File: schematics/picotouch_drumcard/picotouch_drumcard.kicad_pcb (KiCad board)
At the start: 2 copper layers, 88.9 x 63.5 mm, 73 parts, among them J1 AudioJack4, J2 AudioJack4, J3 AudioJack4, SW1 Capacitive Button, SW10 Capacitive Button, SW11 Capacitive Button, SW12 Capacitive Button, SW13 Capacitive Button, SW14 Capacitive Button, SW15 Capacitive Button, SW16 Capacitive Button, SW17 Capacitive Button, SW2 Capacitive Button, SW3 Capacitive Button, SW4 Capacitive Button, SW5 Capacitive Button, SW6 Capacitive Button, SW7 Capacitive Button, SW8 Capacitive Button, SW9 Capacitive Button, U1 Pico, U2 H11L1S(TA), U3 MCP73831-2-OT, U4 TS20, X1 AFC20-S02ACA-00

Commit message: second
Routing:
- net /TOUCH5: track 49.0 -> 49.6 mm
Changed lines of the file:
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@@
 			(layers "B.Cu" "B.Paste" "B.Mask")
 			(net 48 "unconnected-(J3-PadR2)")
-			(pintype "passive")
+			(pintype "passive+no_connect")
 		)
 		(pad "S" smd rect
@@
 			(net 83 "unconnected-(U1-GPIO18-Pad24)")
 			(pinfunction "GPIO18")
-			(pintype "bidirectional")
+			(pintype "bidirectional+no_connect")
 		)
 		(pad "25" smd rect
@@
 			(layers "B.Cu" "B.Paste" "B.Mask")
 			(net 47 "unconnected-(J2-PadR2)")
-			(pintype "passive")
+			(pintype "passive+no_connect")
 		)
 		(pad "S" smd rect
@@
 	)
 	(segment
-		(start 118.11 33.02)
-		(end 156.48125 33.02)
+		(start 118.872 33.782)
+		(end 116.84 31.75)
 		(width 0.2)
 		(layer "B.Cu")
@@
 	)
 	(segment
-		(start 156.48125 33.02)
-		(end 157.319 33.85775)
+		(start 157.319 33.85775)
+		(end 157.319 34.6025)
 		(width 0.2)
 		(layer "B.Cu")
@@
 	)
 	(segment
-		(start 116.84 31.75)
-		(end 118.11 33.02)
+		(start 133.096 33.782)
+		(end 133.858 33.02)
 		(width 0.2)
 		(layer "B.Cu")
@@
 	)
 	(segment
-		(start 157.319 33.85775)
-		(end 157.319 34.6025)
+		(start 133.858 33.02)
+		(end 156.48125 33.02)
+		(width 0.2)
+		(layer "B.Cu")
+		(net 6)
+	)
+	(segment
+		(start 156.48125 33.02)
+		(end 157.319 33.85775)
+		(width 0.2)
+		(layer "B.Cu")
+		(net 6)
+	)
+	(segment
+		(start 133.096 33.782)
+		(end 118.872 33.782)
 		(width 0.2)
 		(layer "B.Cu")
@@
 	)
 	(segment
+		(start 164.592 38.862)
+		(end 161.869 36.139)
+		(width 0.2)
+		(layer "B.Cu")
+		(net 41)
+	)
+	(segment
 		(start 165.1 42.418)
 		(end 165.1 49.022)
@@
 	)
 	(segment
-		(start 164.592 38.862)
-		(end 161.869 36.139)
-		(width 0.2)
-		(layer "B.Cu")
-		(net 41)
-	)
-	(segment
-		(start 165.1 51.562)
-		(end 165.1 44.958)
+		(start 163.576 42.926)
+		(end 163.576 40.894)
 		(width 0.2)
 		(layer "F.Cu")
@@
 	)
 	(segment
-		(start 165.1 44.958)
-		(end 163.83 43.688)
+		(start 163.576 40.894)
+		(end 162.56 39.878)
 		(width 0.2)
 		(layer "F.Cu")
@@
 	)
 	(segment
-		(start 163.83 43.688)
-		(end 163.83 41.148)
+		(start 162.56 39.878)
+		(end 162.56 38.862)
 		(width 0.2)
 		(layer "F.Cu")
@@
 	)
 	(segment
-		(start 163.83 41.148)
-		(end 162.56 39.878)
+		(start 165.1 51.562)
+		(end 165.1 44.45)
 		(width 0.2)
 		(layer "F.Cu")
@@
 	)
 	(segment
-		(start 162.56 39.878)
-		(end 162.56 38.862)
+		(start 119.38 67.31)
+		(end 123.952 71.882)
 		(width 0.2)
 		(layer "F.Cu")
@@
 	)
 	(segment
-		(start 119.38 67.31)
-		(end 123.952 71.882)
+		(start 165.1 44.45)
+		(end 163.576 42.926)
 		(width 0.2)
 		(layer "F.Cu")

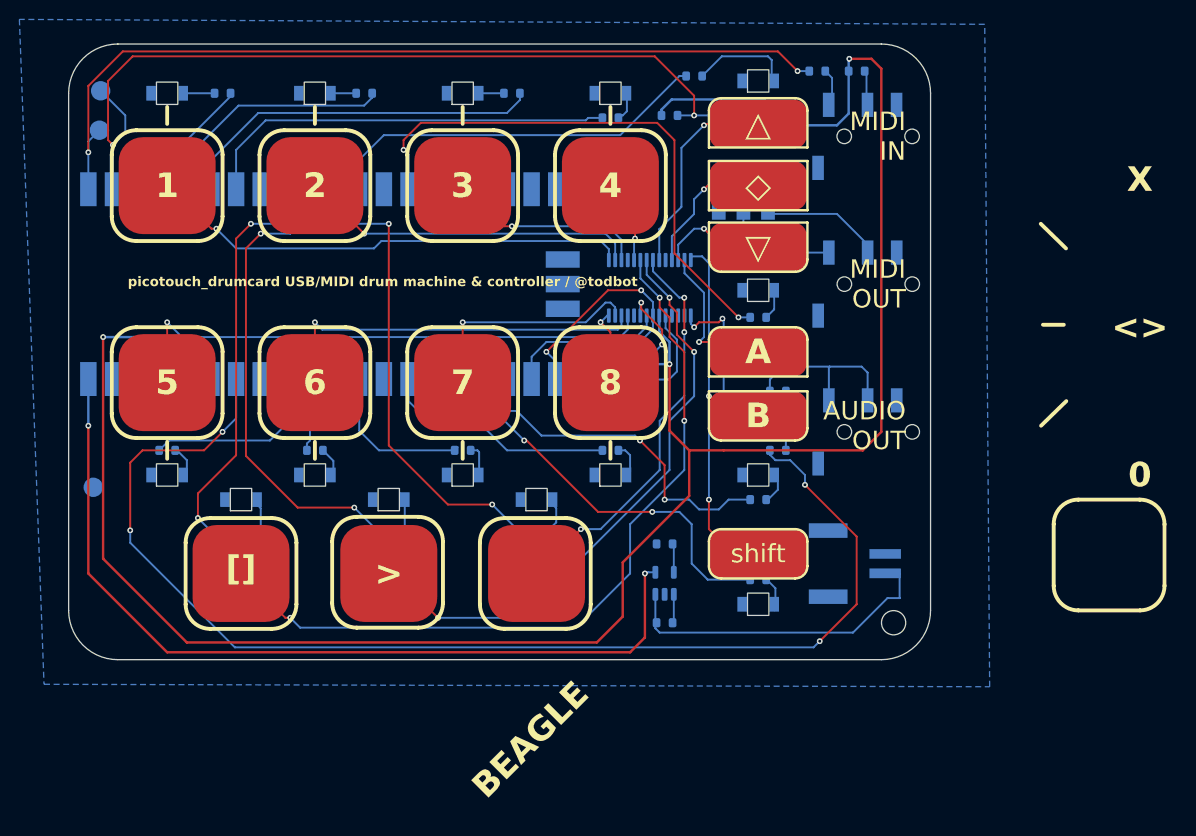
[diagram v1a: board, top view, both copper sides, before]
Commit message: added protection diodes
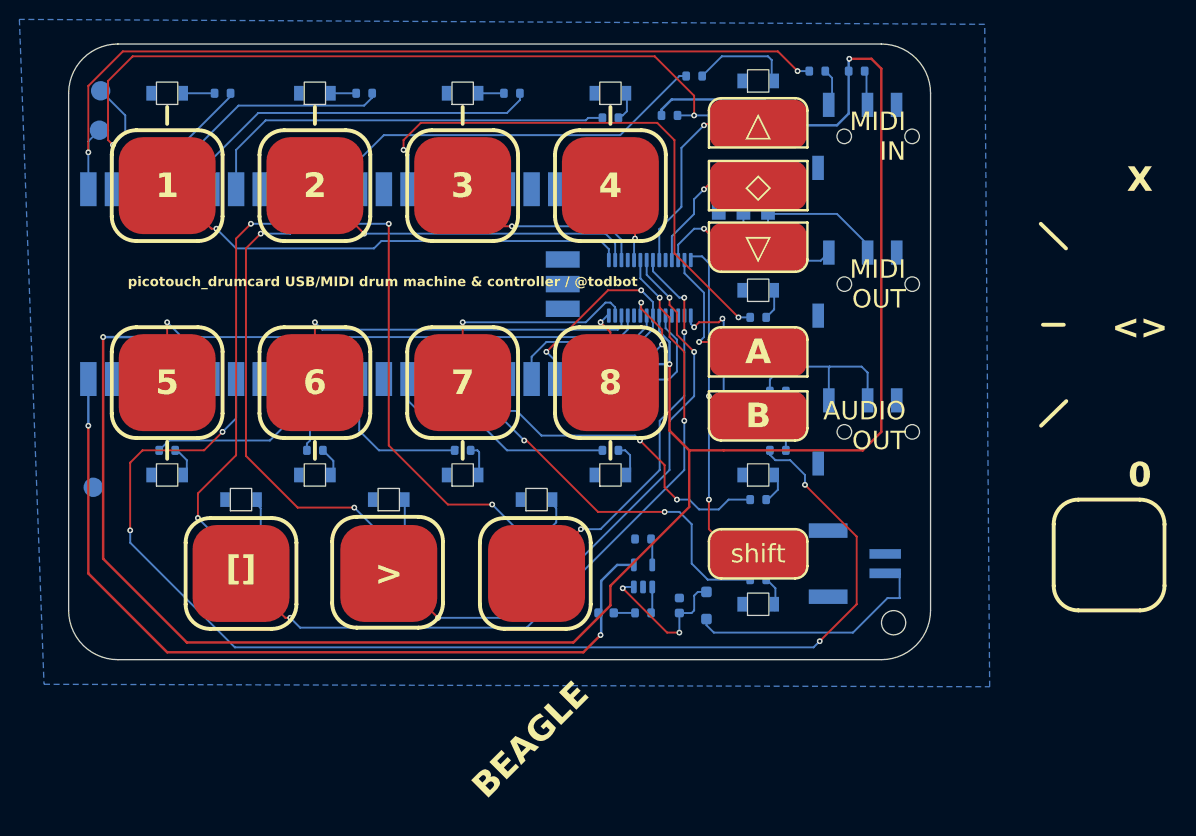
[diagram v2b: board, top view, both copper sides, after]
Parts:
- added C4: 10uF, Capacitor_SMD:C_0603_1608Metric, B.Cu at (164.6, 70.6)
- added D16: 1N4148WT, Diode_SMD:D_SOD-123F, B.Cu at (172.7, 33.7)
- added D17: orange, LED_SMD:LED_0603_1608Metric, B.Cu at (157.0, 71.4)
- added D18: MBR120, Diode_SMD:D_SOD-123F, B.Cu at (167.4, 70.6)
- moved R301 2.44 mm to (160.8, 71.4)
- moved U3 2.35 mm to (160.8, 67.6)
- moved R300 2.28 mm to (160.8, 63.8)
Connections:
- R301 pad 2: +BATT -> Net-(D17-K)
- U3 pad 3: +BATT -> Net-(D18-K)
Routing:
- net Net-(D18-K): track 0.00 -> 15.5 mm, vias 0 -> 2
- net +BATT: track 34.4 -> 26.4 mm
- net Net-(D16-K): track 12.8 -> 16.6 mm
- net /TOUCH9: track 81.7 -> 78.7 mm
- net Net-(D16-A): track 11.8 -> 14.4 mm
- net +5V: track 90.1 -> 87.6 mm
- net Net-(D17-K): track 0.00 -> 2.20 mm
- net +3.3V: track 227.0 -> 225.5 mm
- net /LED14: track 40.5 -> 39.7 mm

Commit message: fix button labels
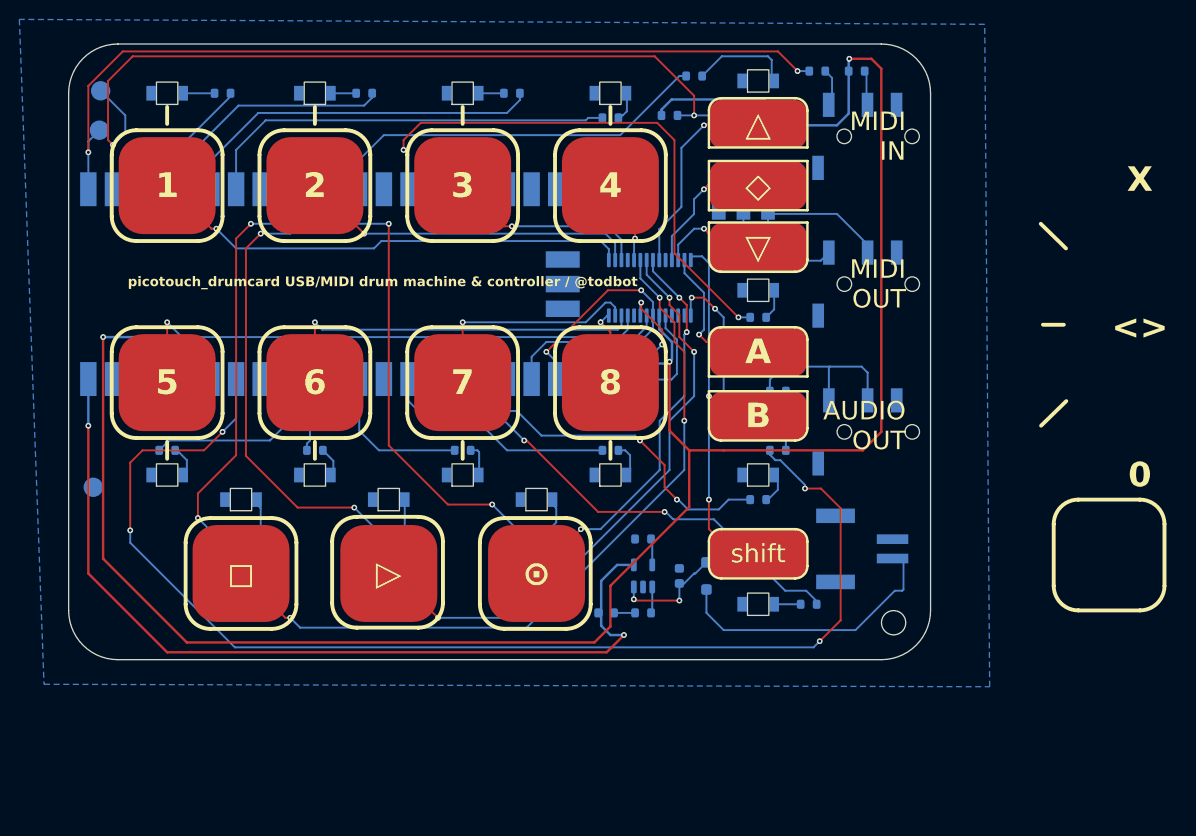
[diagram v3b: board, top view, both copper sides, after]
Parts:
- moved R15 5.79 mm to (177.9, 70.5), turned to 180 degrees
- moved C4 3.05 mm to (164.6, 67.6)
- moved D18 3.05 mm to (167.4, 67.6)
- moved X1 1.70 mm to (183.6, 64.8)
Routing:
- net /LED15: track 46.2 -> 51.5 mm
- net +5V: track 87.6 -> 91.7 mm
- net Net-(D18-K): track 15.5 -> 11.5 mm
- net +BATT: track 26.4 -> 29.5 mm
- net +3.3V: track 225.5 -> 227.1 mm
- net /PWM_AUDIO_OUT: track 127.8 -> 126.7 mm
- net Net-(D15-A): track 3.64 -> 2.79 mm
- net /TOUCH17: track 33.5 -> 34.3 mm
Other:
- board text added: "⊙"
- board text added: "▷"
- board text added: "◻︎"
- board text removed: ">"
- board text removed: "BEAGLE"
- board text removed: "[]"

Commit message: tuning layout
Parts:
- moved C1 1.52 mm to (174.8, 51.6)
- moved R19 1.52 mm to (174.8, 53.1)
- moved R20 1.52 mm to (174.8, 50.0)
- moved R21 1.52 mm to (174.8, 47.0)
- moved C2 1.52 mm to (174.8, 48.5)
- moved D13 1.02 mm to (172.7, 39.1)
- moved R13 1.02 mm to (172.7, 41.9)
- moved D12 0.76 mm to (172.7, 15.7)
- moved D14 0.76 mm to (172.7, 56.4)
- renumbered R100 to R17, R101 to R18, R200 to R19, R201 to R20, R202 to R21, R203 to R22, R204 to R23, R205 to R24
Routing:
- net /PWM_AUDIO_OUT: track 126.7 -> 130.0 mm
- net /LED13: track 57.8 -> 58.8 mm
- net Net-(D14-A): track 3.31 -> 4.07 mm
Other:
- board text removed: "0"
- board text removed: "<>"
- board text removed: "X"

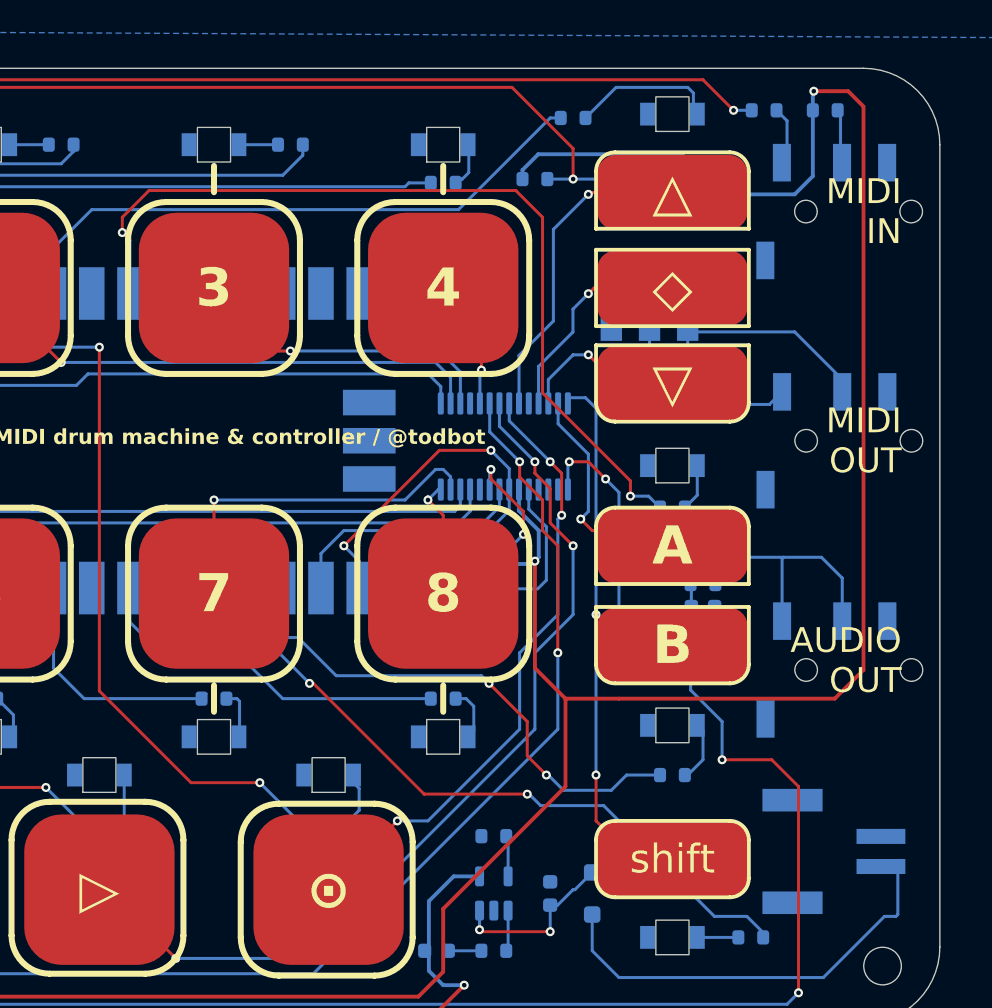
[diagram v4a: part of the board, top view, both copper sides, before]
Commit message: add missing cap on opto
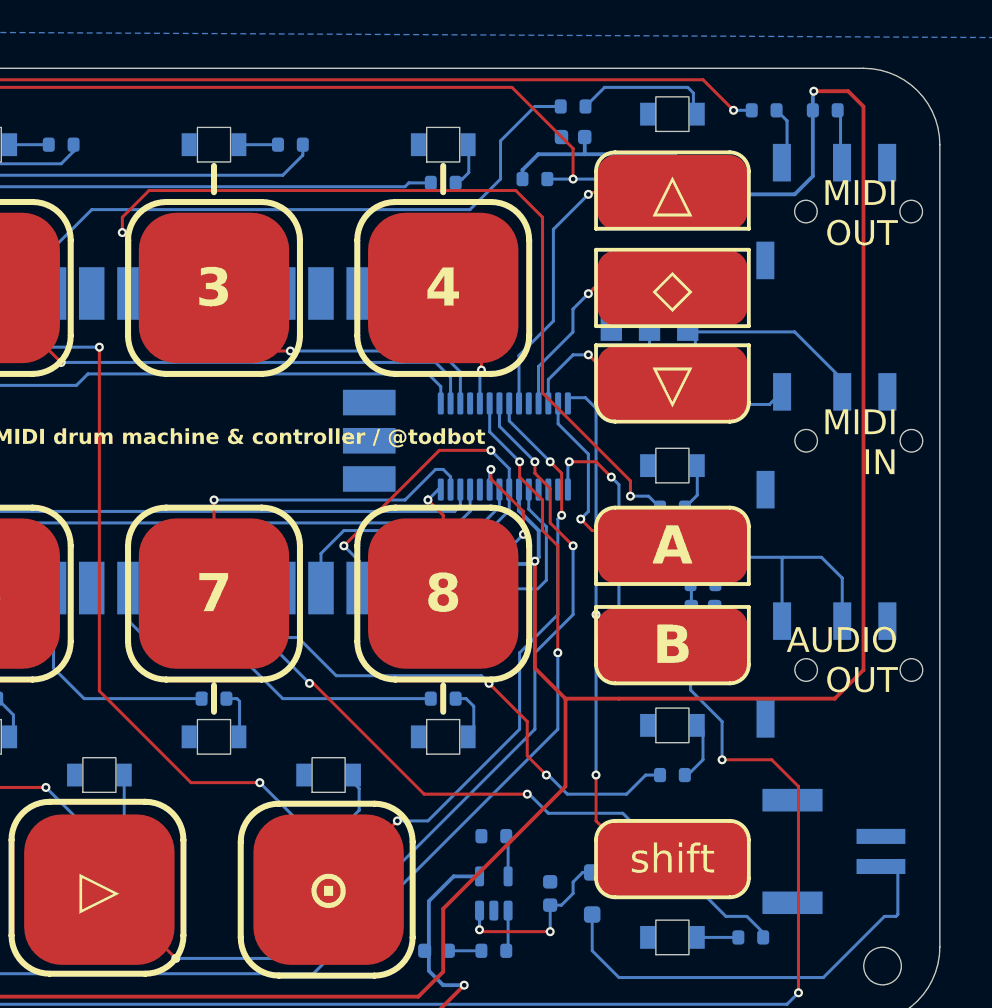
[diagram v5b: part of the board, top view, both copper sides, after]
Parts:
- added C5: 100n, Capacitor_SMD:C_0603_1608Metric, B.Cu at (166.1, 17.3)
- moved R12 0.76 mm to (166.1, 15.2)
- renumbered R300 to R25, R301 to R26
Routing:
- net /LED12: track 41.2 -> 43.0 mm
- net Net-(D16-K): track 16.6 -> 17.3 mm

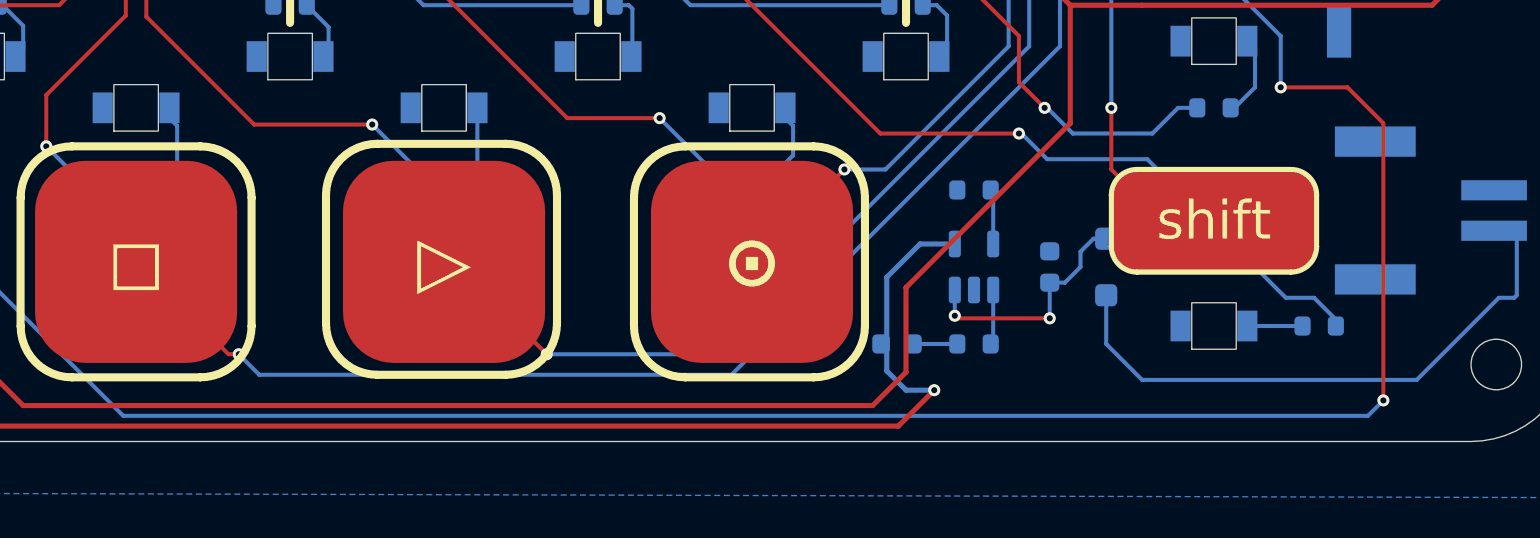
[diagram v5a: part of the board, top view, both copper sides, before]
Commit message: dangit forgot power switch
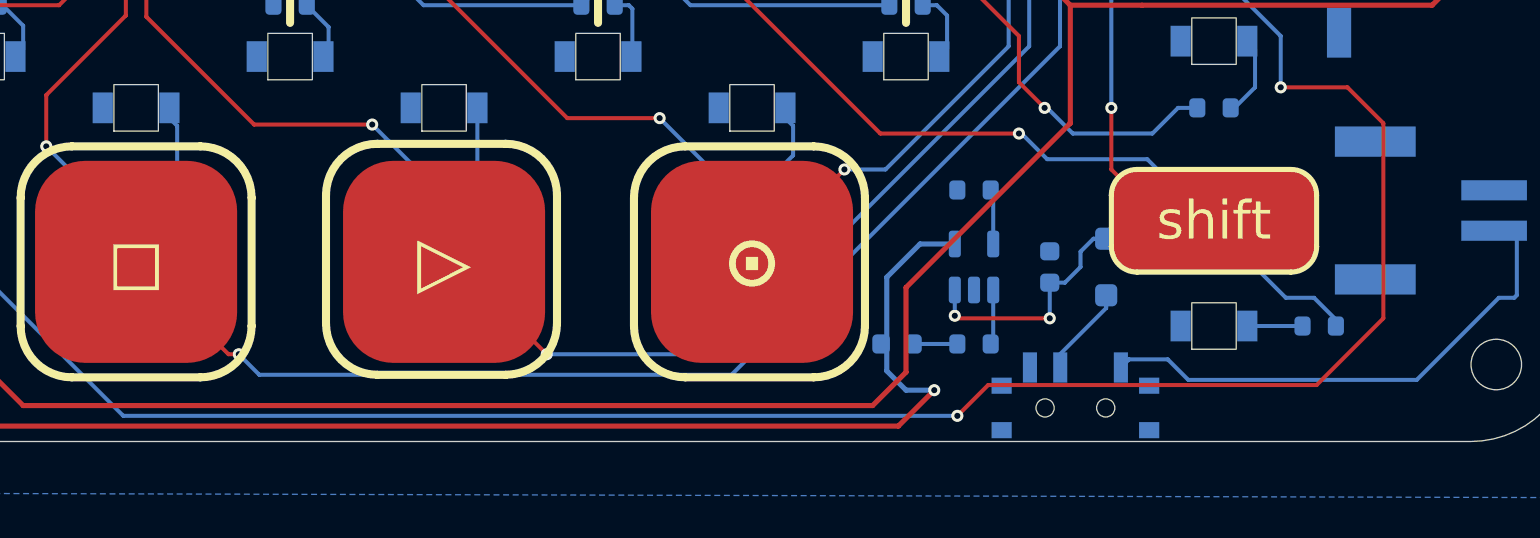
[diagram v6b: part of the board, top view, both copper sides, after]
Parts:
- added SW18: SSSS811101, easyeda2kicad:SW-SMD_SSSS811101, B.Cu at (165.9, 74.1)
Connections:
- D18 pad 2: +BATT -> Net-(D18-A)
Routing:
- net Net-(D18-A): track 0.00 -> 4.52 mm
- net +BATT: track 29.5 -> 26.2 mm
- net /PWM_AUDIO_OUT: track 130.0 -> 127.6 mm
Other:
- board text added: "picotouch_drumcard 2 Aug 2024 - @todbot / Tod Kurt github.com/todbot/picotouch_drumcard"
- board text removed: "picotouch_drumcard 30 Jul 2024 - @todbot / Tod Kurt github.com/todbot/picotouch_drumcard"
